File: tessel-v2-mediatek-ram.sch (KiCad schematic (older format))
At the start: 22 parts, among them U201 MT7620N, U301 W9751G6KB-25

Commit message: 0603 resistor swapped
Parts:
- C301, C302, C303, C304, C305, C306, C307, C308, C309, C310, C311, C312, C313, C314, C315: footprint tm-kicad-lib:SMD-0402 -> tm-kicad-lib:SMD-0402-C
- R301, R302, R303, R304, R305: footprint tm-kicad-lib:SMD-0402 -> tm-kicad-lib:SMD-0402-R
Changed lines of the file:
@@
 LIBS:valves
 LIBS:tm-kicad-lib
+LIBS:nordicsemi
 LIBS:tessel-v2-cache
 EELAYER 25 0
@@
 F 0 "C306" H 13400 5700 40  0000 L CNN
 F 1 "10nF" H 13406 5515 40  0000 L CNN
-F 2 "tm-kicad-lib:SMD-0402" H 13438 5450 30  0001 C CNN
+F 2 "tm-kicad-lib:SMD-0402-C" H 13438 5450 30  0001 C CNN
 F 3 "" H 13400 5600 60  0000 C CNN
 	1    13400 5600
@@
 F 0 "R303" V 7730 4300 40  0000 C CNN
 F 1 "120R" V 7657 4301 40  0000 C CNN
-F 2 "tm-kicad-lib:SMD-0402" V 7580 4300 30  0001 C CNN
+F 2 "tm-kicad-lib:SMD-0402-R" V 7580 4300 30  0001 C CNN
 F 3 "" H 7650 4300 30  0000 C CNN
 	1    7650 4300
@@
 F 0 "R301" V 6930 4050 40  0000 C CNN
 F 1 "22R" V 6857 4051 40  0000 C CNN
-F 2 "tm-kicad-lib:SMD-0402" V 6780 4050 30  0001 C CNN
+F 2 "tm-kicad-lib:SMD-0402-R" V 6780 4050 30  0001 C CNN
 F 3 "" H 6850 4050 30  0000 C CNN
 	1    6850 4050
@@
 F 0 "R302" V 6930 4250 40  0000 C CNN
 F 1 "22R" V 6857 4251 40  0000 C CNN
-F 2 "tm-kicad-lib:SMD-0402" V 6780 4250 30  0001 C CNN
+F 2 "tm-kicad-lib:SMD-0402-R" V 6780 4250 30  0001 C CNN
 F 3 "" H 6850 4250 30  0000 C CNN
 	1    6850 4250
@@
 F 0 "C302" H 7400 4650 40  0000 L CNN
 F 1 "5pF" H 7406 4465 40  0000 L CNN
-F 2 "tm-kicad-lib:SMD-0402" H 7438 4400 30  0001 C CNN
+F 2 "tm-kicad-lib:SMD-0402-C" H 7438 4400 30  0001 C CNN
 F 3 "" H 7400 4550 60  0000 C CNN
 	1    7400 4550
@@
 F 0 "C301" H 7200 4650 40  0000 L CNN
 F 1 "5pF" H 7206 4465 40  0000 L CNN
-F 2 "tm-kicad-lib:SMD-0402" H 7238 4400 30  0001 C CNN
+F 2 "tm-kicad-lib:SMD-0402-C" H 7238 4400 30  0001 C CNN
 F 3 "" H 7200 4550 60  0000 C CNN
 	1    7200 4550
@@
 F 0 "C304" H 9400 9000 40  0000 L CNN
 F 1 "100nF" H 9406 8815 40  0000 L CNN
-F 2 "tm-kicad-lib:SMD-0402" H 9438 8750 30  0001 C CNN
+F 2 "tm-kicad-lib:SMD-0402-C" H 9438 8750 30  0001 C CNN
 F 3 "" H 9400 8900 60  0000 C CNN
 	1    9400 8900
@@
 F 0 "R304" V 9480 8350 40  0000 C CNN
 F 1 "4.7kR 1%" V 9407 8351 40  0000 C CNN
-F 2 "tm-kicad-lib:SMD-0402" V 9330 8350 30  0001 C CNN
+F 2 "tm-kicad-lib:SMD-0402-R" V 9330 8350 30  0001 C CNN
 F 3 "" H 9400 8350 30  0000 C CNN
 	1    9400 8350
@@
 F 0 "R305" V 9830 8600 40  0000 C CNN
 F 1 "4.7kR 1%" V 9757 8601 40  0000 C CNN
-F 2 "tm-kicad-lib:SMD-0402" V 9680 8600 30  0001 C CNN
+F 2 "tm-kicad-lib:SMD-0402-R" V 9680 8600 30  0001 C CNN
 F 3 "" H 9750 8600 30  0000 C CNN
 	1    9750 8600
@@
 F 0 "C303" H 9400 8250 40  0000 L CNN
 F 1 "100nF" H 9406 8065 40  0000 L CNN
-F 2 "tm-kicad-lib:SMD-0402" H 9438 8000 30  0001 C CNN
+F 2 "tm-kicad-lib:SMD-0402-C" H 9438 8000 30  0001 C CNN
 F 3 "" H 9400 8150 60  0000 C CNN
 	1    9400 8150
@@
 F 0 "C305" H 9950 8700 40  0000 L CNN
 F 1 "100nF" H 9956 8515 40  0000 L CNN
-F 2 "tm-kicad-lib:SMD-0402" H 9988 8450 30  0001 C CNN
+F 2 "tm-kicad-lib:SMD-0402-C" H 9988 8450 30  0001 C CNN
 F 3 "" H 9950 8600 60  0000 C CNN
 	1    9950 8600
@@
 F 0 "C307" H 13650 5700 40  0000 L CNN
 F 1 "100nF" H 13656 5515 40  0000 L CNN
-F 2 "tm-kicad-lib:SMD-0402" H 13688 5450 30  0001 C CNN
+F 2 "tm-kicad-lib:SMD-0402-C" H 13688 5450 30  0001 C CNN
 F 3 "" H 13650 5600 60  0000 C CNN
 	1    13650 5600
@@
 F 0 "C308" H 13900 5700 40  0000 L CNN
 F 1 "100nF" H 13906 5515 40  0000 L CNN
-F 2 "tm-kicad-lib:SMD-0402" H 13938 5450 30  0001 C CNN
+F 2 "tm-kicad-lib:SMD-0402-C" H 13938 5450 30  0001 C CNN
 F 3 "" H 13900 5600 60  0000 C CNN
 	1    13900 5600
@@
 F 0 "C309" H 14150 5700 40  0000 L CNN
 F 1 "100nF" H 14156 5515 40  0000 L CNN
-F 2 "tm-kicad-lib:SMD-0402" H 14188 5450 30  0001 C CNN
+F 2 "tm-kicad-lib:SMD-0402-C" H 14188 5450 30  0001 C CNN
 F 3 "" H 14150 5600 60  0000 C CNN
 	1    14150 5600
@@
 F 0 "C310" H 14400 5700 40  0000 L CNN
 F 1 "100nF" H 14406 5515 40  0000 L CNN
-F 2 "tm-kicad-lib:SMD-0402" H 14438 5450 30  0001 C CNN
+F 2 "tm-kicad-lib:SMD-0402-C" H 14438 5450 30  0001 C CNN
 F 3 "" H 14400 5600 60  0000 C CNN
 	1    14400 5600
@@
 F 0 "C311" H 13400 7050 40  0000 L CNN
 F 1 "10nF" H 13406 6865 40  0000 L CNN
-F 2 "tm-kicad-lib:SMD-0402" H 13438 6800 30  0001 C CNN
+F 2 "tm-kicad-lib:SMD-0402-C" H 13438 6800 30  0001 C CNN
 F 3 "" H 13400 6950 60  0000 C CNN
 	1    13400 6950
@@
 F 0 "C312" H 13650 7050 40  0000 L CNN
 F 1 "100nF" H 13656 6865 40  0000 L CNN
-F 2 "tm-kicad-lib:SMD-0402" H 13688 6800 30  0001 C CNN
+F 2 "tm-kicad-lib:SMD-0402-C" H 13688 6800 30  0001 C CNN
 F 3 "" H 13650 6950 60  0000 C CNN
 	1    13650 6950
@@
 F 0 "C313" H 13900 7050 40  0000 L CNN
 F 1 "100nF" H 13906 6865 40  0000 L CNN
-F 2 "tm-kicad-lib:SMD-0402" H 13938 6800 30  0001 C CNN
+F 2 "tm-kicad-lib:SMD-0402-C" H 13938 6800 30  0001 C CNN
 F 3 "" H 13900 6950 60  0000 C CNN
 	1    13900 6950
@@
 F 0 "C314" H 14150 7050 40  0000 L CNN
 F 1 "100nF" H 14156 6865 40  0000 L CNN
-F 2 "tm-kicad-lib:SMD-0402" H 14188 6800 30  0001 C CNN
+F 2 "tm-kicad-lib:SMD-0402-C" H 14188 6800 30  0001 C CNN
 F 3 "" H 14150 6950 60  0000 C CNN
 	1    14150 6950
@@
 F 0 "C315" H 14400 7050 40  0000 L CNN
 F 1 "100nF" H 14406 6865 40  0000 L CNN
-F 2 "tm-kicad-lib:SMD-0402" H 14438 6800 30  0001 C CNN
+F 2 "tm-kicad-lib:SMD-0402-C" H 14438 6800 30  0001 C CNN
 F 3 "" H 14400 6950 60  0000 C CNN
 	1    14400 6950

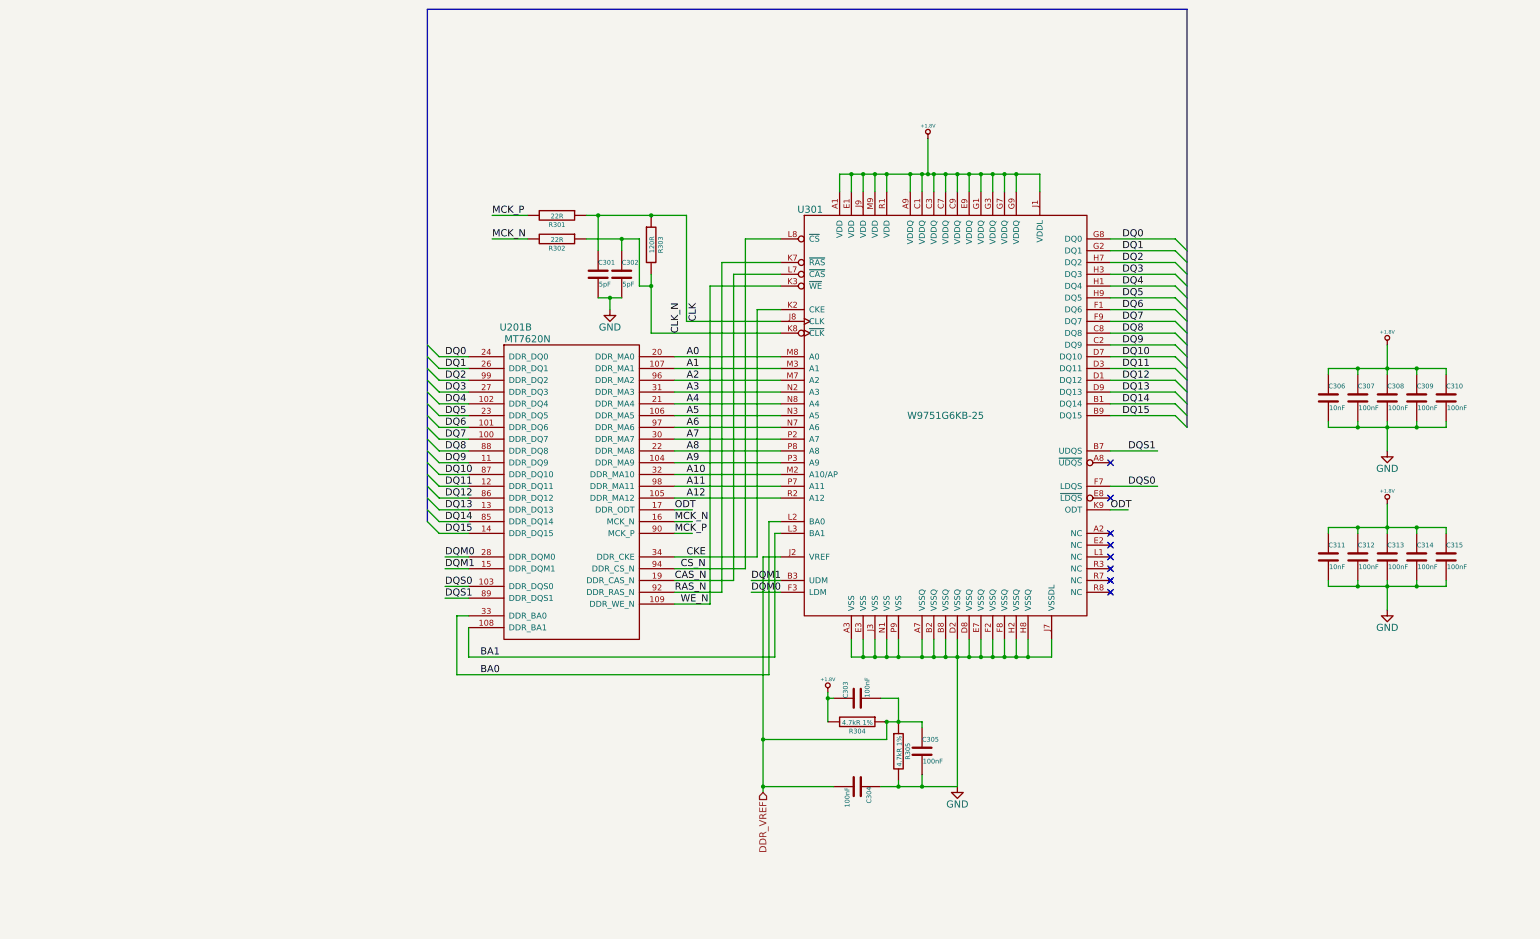
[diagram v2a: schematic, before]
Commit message: working towards pin muxing for v2v3 and general schematic cleanup
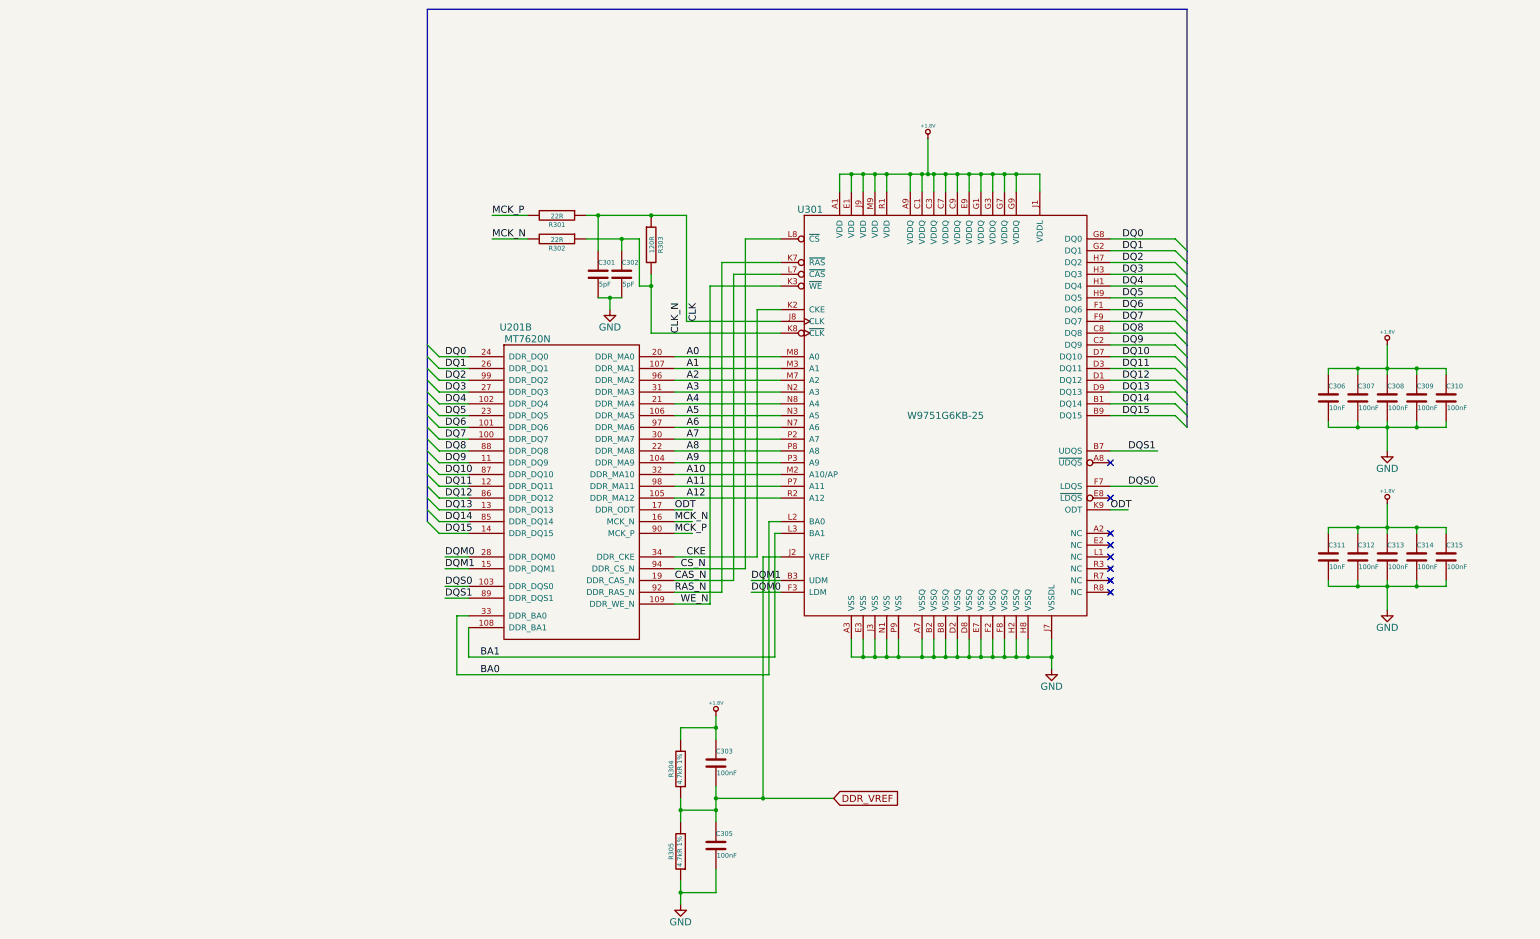
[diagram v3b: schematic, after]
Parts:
- removed C304: 100nF, tm-kicad-lib:SMD-0402-C, symbol C
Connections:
- wire segments 168 -> 224
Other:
- moved on the sheet: C303, C305, R304, R305

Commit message: most schematic changes done, major refactoring underway
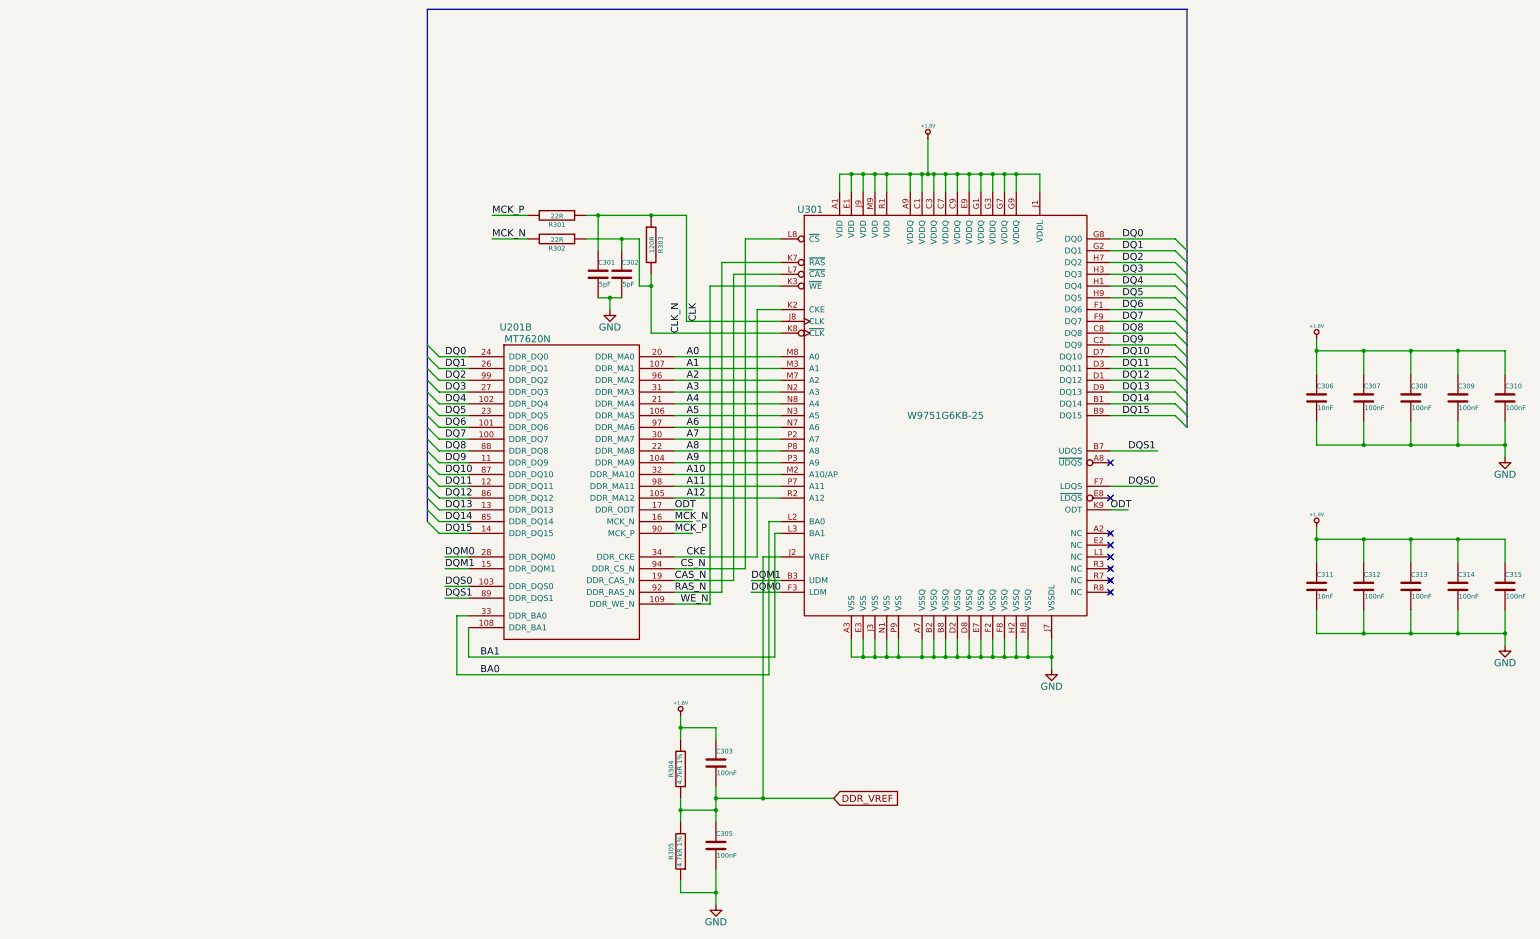
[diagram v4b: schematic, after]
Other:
- moved on the sheet: C306, C307, C308, C309, C310, C311, C312, C313, C314, C315

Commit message: still refactoring. usb is a pain
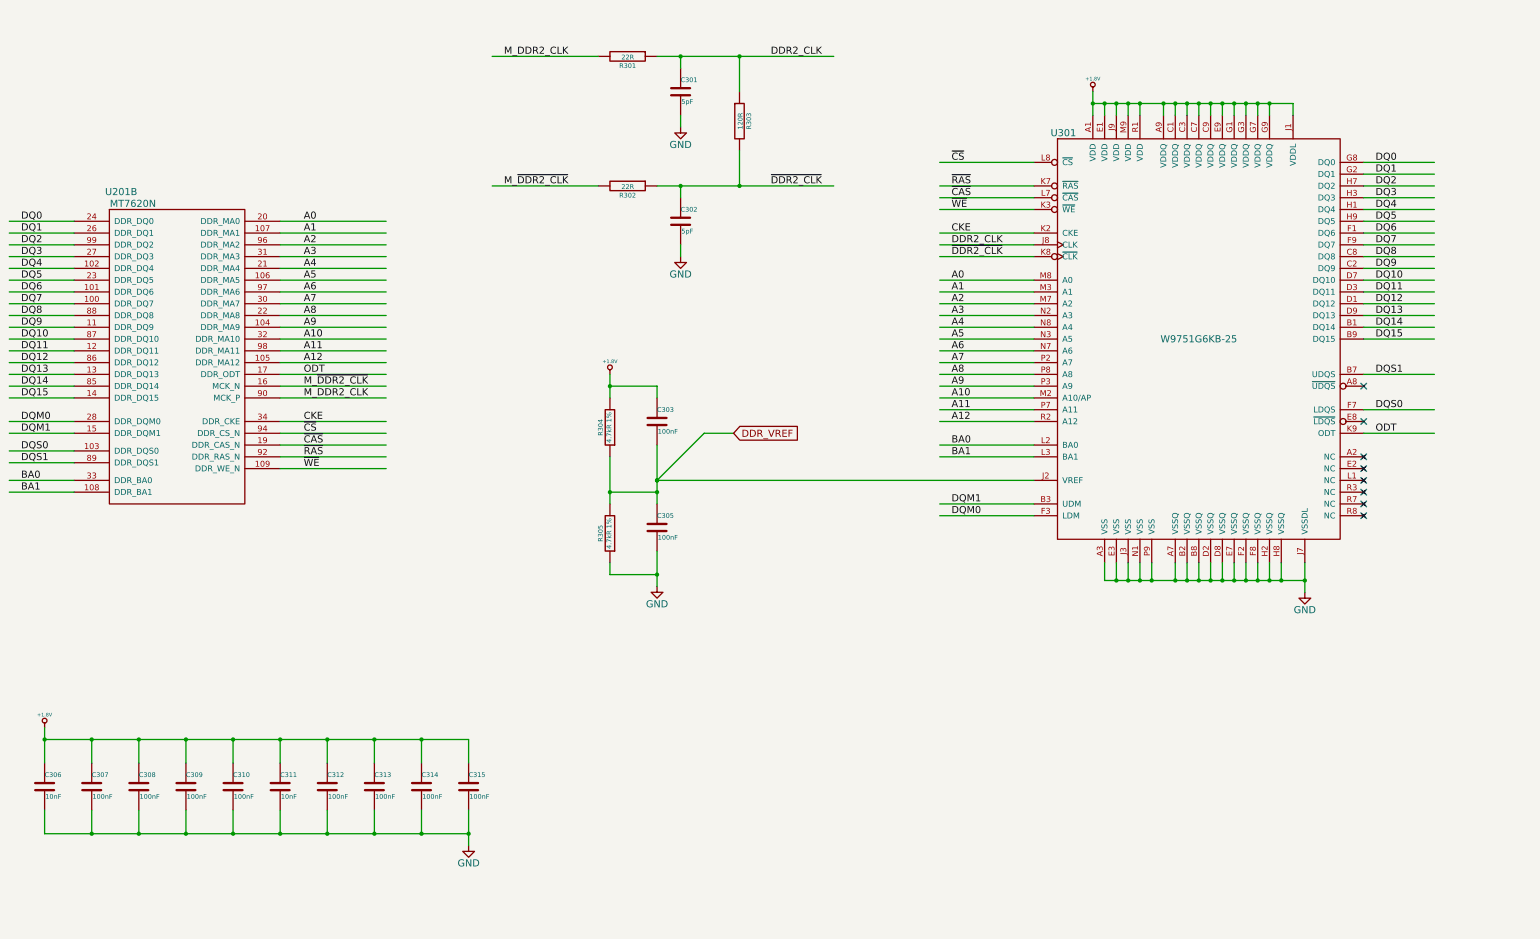
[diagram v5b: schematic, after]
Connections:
- net labels added: DDR2_CLK, M_DDR2_CLK, M_~DDR2_CLK, ~CAS, ~CS, ~DDR2_CLK, ~RAS, ~WE
- net labels removed: CAS_N, CLK, CLK_N, CS_N, MCK_N, MCK_P, RAS_N, WE_N
- wire segments 223 -> 222
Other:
- moved on the sheet: C301, C302, C303, C305, C306, C307, C308, C309, C310, C311, C312, C313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
